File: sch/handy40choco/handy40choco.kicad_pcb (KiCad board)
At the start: 2 copper layers, 169 x 71 mm, 95 parts, among them J1 Conn_01x20, SW1 SW_Push, SW10 SW_Push, SW11 SW_Push, SW12 SW_Push, SW13 SW_Push, SW14 SW_Push, SW15 SW_Push, SW16 SW_Push, SW17 SW_Push, SW18 SW_Push, SW19 SW_Push, SW2 SW_Push, SW20 SW_Push, SW21 SW_Push, SW22 SW_Push, SW23 SW_Push, SW24 SW_Push, SW25 SW_Push, SW26 SW_Push, SW27 SW_Push, SW28 SW_Push, SW29 SW_Push, SW3 SW_Push, SW30 SW_Push, SW31 SW_Push, SW32 SW_Push, SW33 SW_Push, SW34 SW_Push, SW35 SW_Push, SW36 SW_Push, SW37 SW_Push, SW38 SW_Push, SW39 SW_Push, SW4 SW_Push, SW40 SW_Push, SW5 SW_Push, SW6 SW_Push, SW7 SW_Push, SW8 SW_Push, SW9 SW_Push

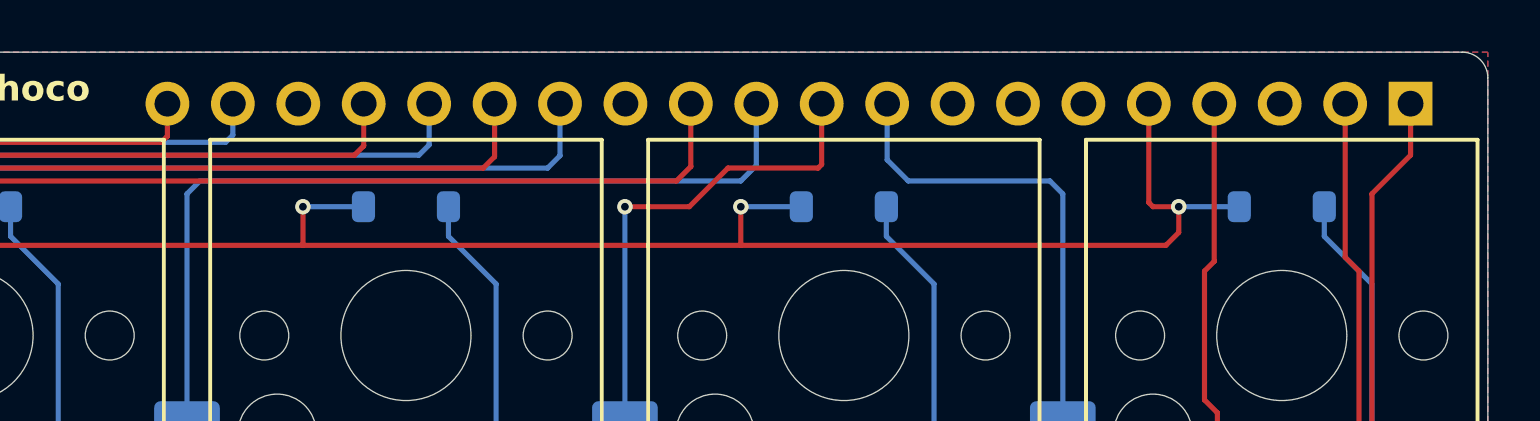
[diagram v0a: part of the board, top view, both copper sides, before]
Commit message: ピンヘッダのフットプリントをコンスルーが使えるように、Φ0.85に変更しました。
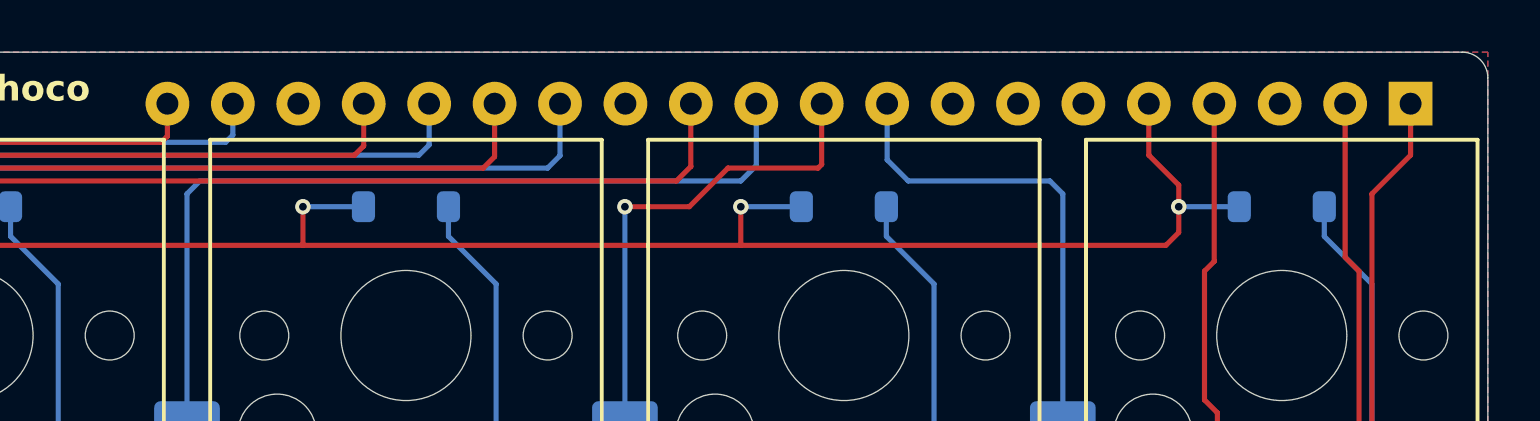
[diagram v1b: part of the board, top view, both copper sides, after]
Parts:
- J1: footprint Connector_PinHeader_2.54mm:PinHeader_1x20_P2.54mm_Vertical -> my_keyswitch:my_PinHeader_1x20_P2.54mm_Vertical_p0.85
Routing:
- net /ROW0: track 200.8 -> 200.2 mm
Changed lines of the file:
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@@
 		)
 	)
-	(footprint "Connector_PinHeader_2.54mm:PinHeader_1x20_P2.54mm_Vertical"
+	(footprint "my_keyswitch:my_PinHeader_1x20_P2.54mm_Vertical_p0.85"
 		(layer "B.Cu")
 		(at 207 88 90)
@@
 		(tags "Through hole pin header THT 1x20 2.54mm single row")
 		(property "Reference" "J1"
-			(at 0 2.38 90)
+			(at 0 2.38 270)
 			(layer "B.SilkS")
 			(effects
@@
 		)
 		(property "Value" "Conn_01x20"
-			(at 0 -50.64 90)
+			(at 0 -50.64 270)
 			(layer "B.Fab")
 			(effects
@@
 		)
 		(property "Datasheet" ""
-			(at 0 0 90)
+			(at 0 0 270)
 			(layer "B.Fab")
 			(hide yes)
@@
 		)
 		(property "Description" "Generic connector, single row, 01x20, script generated (kicad-library-utils/schlib/autogen/connector/)"
-			(at 0 0 90)
+			(at 0 0 270)
 			(layer "B.Fab")
 			(hide yes)
@@
 			(at 0 0 90)
 			(size 1.7 1.7)
-			(drill 1)
+			(drill 0.85)
 			(layers "*.Cu" "*.Mask")
 			(remove_unused_layers no)
@@
 			(at 0 -2.54 90)
 			(size 1.7 1.7)
-			(drill 1)
+			(drill 0.85)
 			(layers "*.Cu" "*.Mask")
 			(remove_unused_layers no)
@@
 			(at 0 -5.08 90)
 			(size 1.7 1.7)
-			(drill 1)
+			(drill 0.85)
 			(layers "*.Cu" "*.Mask")
 			(remove_unused_layers no)
@@
 			(at 0 -7.62 90)
 			(size 1.7 1.7)
-			(drill 1)
+			(drill 0.85)
 			(layers "*.Cu" "*.Mask")
 			(remove_unused_layers no)
@@
 			(at 0 -10.16 90)
 			(size 1.7 1.7)
-			(drill 1)
+			(drill 0.85)
 			(layers "*.Cu" "*.Mask")
 			(remove_unused_layers no)
@@
 			(at 0 -12.7 90)
 			(size 1.7 1.7)
-			(drill 1)
+			(drill 0.85)
 			(layers "*.Cu" "*.Mask")
 			(remove_unused_layers no)
@@
 			(at 0 -15.24 90)
 			(size 1.7 1.7)
-			(drill 1)
+			(drill 0.85)
 			(layers "*.Cu" "*.Mask")
 			(remove_unused_layers no)
@@
 			(at 0 -17.78 90)
 			(size 1.7 1.7)
-			(drill 1)
+			(drill 0.85)
 			(layers "*.Cu" "*.Mask")
 			(remove_unused_layers no)
@@
 			(at 0 -20.32 90)
 			(size 1.7 1.7)
-			(drill 1)
+			(drill 0.85)
 			(layers "*.Cu" "*.Mask")
 			(remove_unused_layers no)
@@
 			(at 0 -22.86 90)
 			(size 1.7 1.7)
-			(drill 1)
+			(drill 0.85)
 			(layers "*.Cu" "*.Mask")
 			(remove_unused_layers no)
@@
 			(at 0 -25.4 90)
 			(size 1.7 1.7)
-			(drill 1)
+			(drill 0.85)
 			(layers "*.Cu" "*.Mask")
 			(remove_unused_layers no)
@@
 			(at 0 -27.94 90)
 			(size 1.7 1.7)
-			(drill 1)
+			(drill 0.85)
 			(layers "*.Cu" "*.Mask")
 			(remove_unused_layers no)
@@
 			(at 0 -30.48 90)
 			(size 1.7 1.7)
-			(drill 1)
+			(drill 0.85)
 			(layers "*.Cu" "*.Mask")
 			(remove_unused_layers no)
@@
 			(at 0 -33.02 90)
 			(size 1.7 1.7)
-			(drill 1)
+			(drill 0.85)
 			(layers "*.Cu" "*.Mask")
 			(remove_unused_layers no)
@@
 			(at 0 -35.56 90)
 			(size 1.7 1.7)
-			(drill 1)
+			(drill 0.85)
 			(layers "*.Cu" "*.Mask")
 			(remove_unused_layers no)
@@
 			(at 0 -38.1 90)
 			(size 1.7 1.7)
-			(drill 1)
+			(drill 0.85)
 			(layers "*.Cu" "*.Mask")
 			(remove_unused_layers no)
@@
 			(at 0 -40.64 90)
 			(size 1.7 1.7)
-			(drill 1)
+			(drill 0.85)
 			(layers "*.Cu" "*.Mask")
 			(remove_unused_layers no)
@@
 			(at 0 -43.18 90)
 			(size 1.7 1.7)
-			(drill 1)
+			(drill 0.85)
 			(layers "*.Cu" "*.Mask")
 			(remove_unused_layers no)
@@
 			(at 0 -45.72 90)
 			(size 1.7 1.7)
-			(drill 1)
+			(drill 0.85)
 			(layers "*.Cu" "*.Mask")
 			(remove_unused_layers no)
@@
 			(at 0 -48.26 90)
 			(size 1.7 1.7)
-			(drill 1)
+			(drill 0.85)
 			(layers "*.Cu" "*.Mask")
 			(remove_unused_layers no)
@@
 			)
 			(rotate
-				(xyz -0 -0 -0)
+				(xyz 0 0 0)
 			)
 		)
@@
 			)
 			(rotate
-				(xyz -0 -180 -0)
+				(xyz -0 180 -0)
 			)
 		)
@@
 	)
 	(segment
+		(start 198 91.16)
+		(end 198 92)
+		(width 0.2)
+		(layer "F.Cu")
+		(net 44)
+	)
+	(segment
 		(start 62 93.5)
 		(end 58 93.5)
@@
 	)
 	(segment
-		(start 197 92)
-		(end 198 92)
-		(width 0.2)
-		(layer "F.Cu")
-		(net 44)
-	)
-	(segment
 		(start 96 92)
 		(end 96 93.5)
@@
 	)
 	(segment
-		(start 196.84 91.84)
-		(end 197 92)
-		(width 0.2)
-		(layer "F.Cu")
-		(net 44)
-	)
-	(segment
 		(start 62 93.5)
 		(end 79 93.5)
@@
 	)
 	(segment
+		(start 196.84 90)
+		(end 198 91.16)
+		(width 0.2)
+		(layer "F.Cu")
+		(net 44)
+	)
+	(segment
 		(start 196.84 88)
-		(end 196.84 91.84)
+		(end 196.84 90)
 		(width 0.2)
 		(layer "F.Cu")

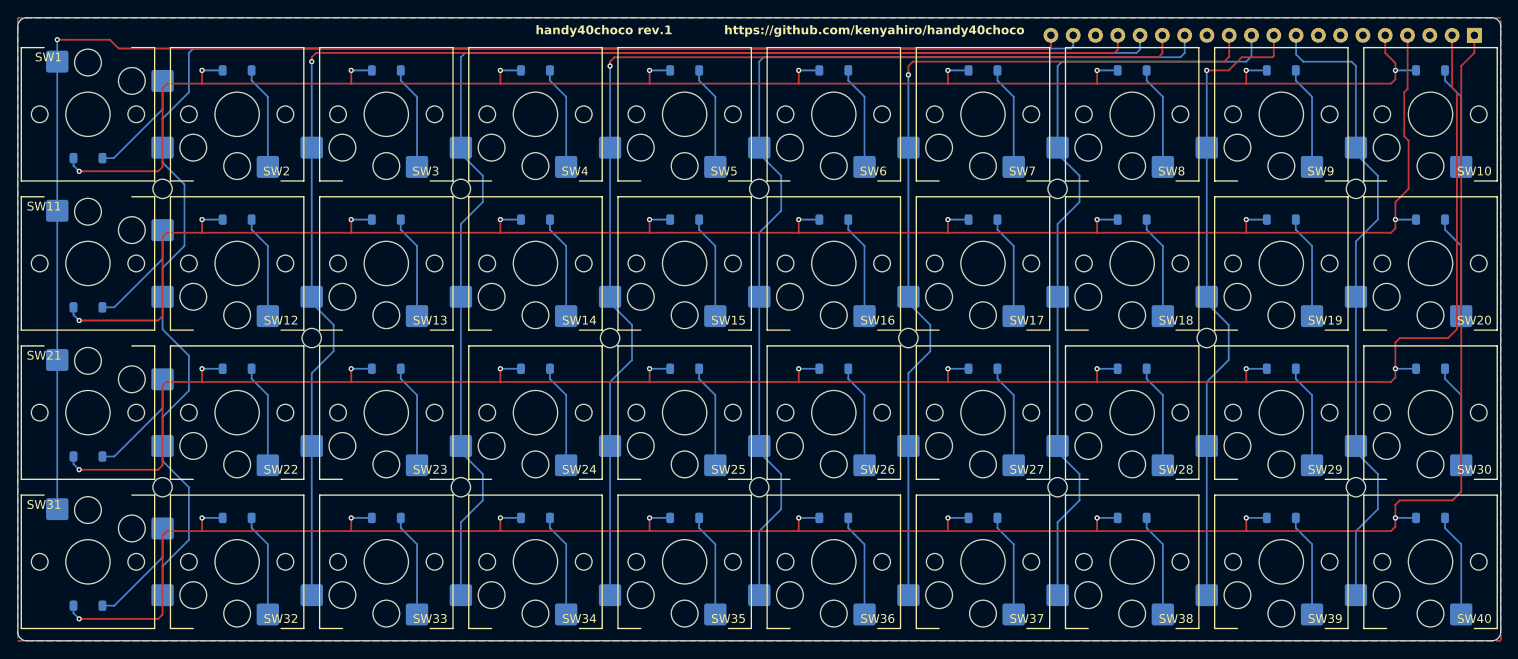
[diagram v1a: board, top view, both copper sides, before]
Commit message: マイコンのピンヘッダの位置を基板端から1.27mmに移動しました。 COLの配線を部品面に移動しました。 基板サイズの微調整を行いました。
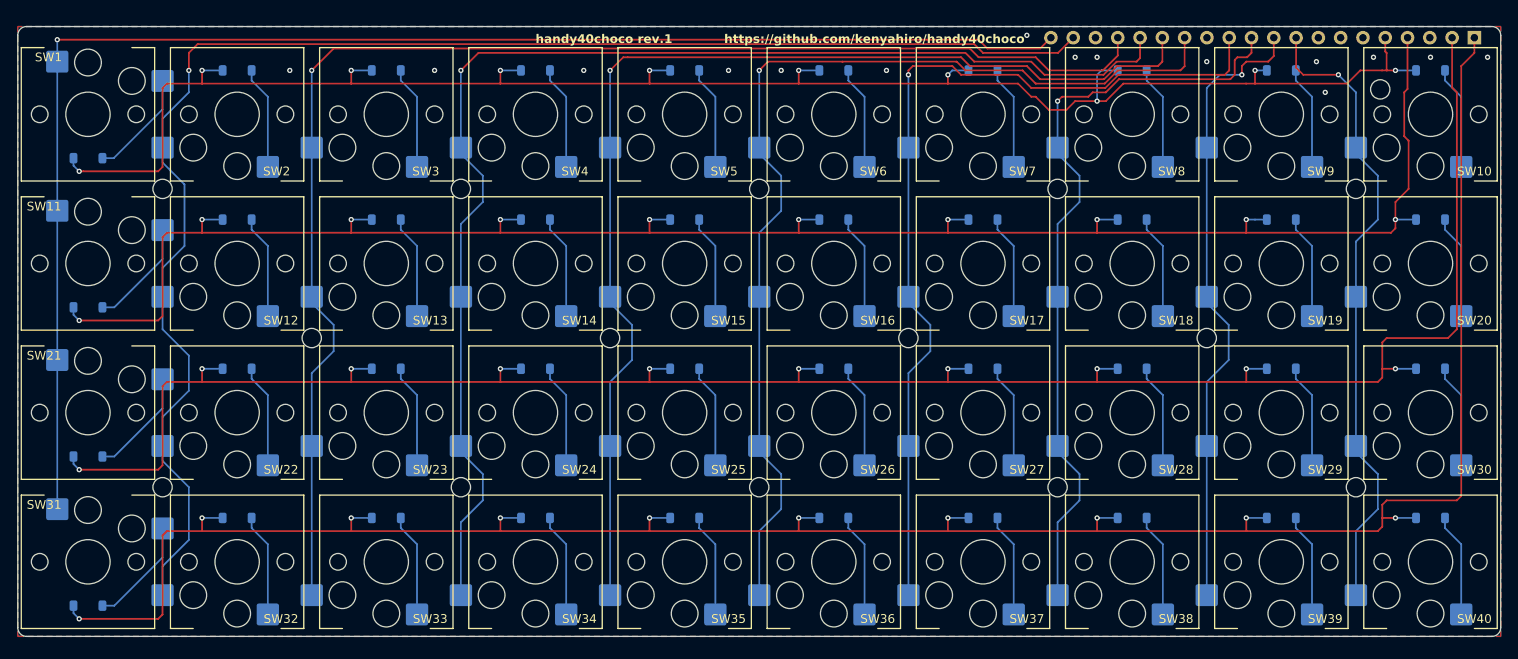
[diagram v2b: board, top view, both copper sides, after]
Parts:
- added H15: MountingHole, my_keyswitch:my_MountingHole_2.2mm_M2, F.Cu at (196.3, 94.2)
- moved J1 0.27 mm to (207.0, 88.3)
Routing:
- net /COL6: track 101.8 -> 104.2 mm
- net /COL5: track 115.8 -> 117.9 mm, vias 0 -> 1
- net /COL7: track 89.4 -> 87.5 mm, vias 0 -> 1
- net /ROW3: track 257.8 -> 259.6 mm
- net /COL4: track 128.3 -> 130.0 mm
- net /ROW0: track 200.2 -> 201.8 mm
- net /COL3: track 144.8 -> 146.3 mm, vias 0 -> 1
- net /ROW2: track 239.9 -> 241.4 mm
- net /COL2: track 157.2 -> 158.5 mm
- net /COL9: track 74.0 -> 72.8 mm, vias 0 -> 1
- net /COL8: track 72.6 -> 71.7 mm
- net /COL0: track 168.5 -> 167.7 mm
- net /COL1: vias 0 -> 1
- net GND: vias 0 -> 15
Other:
- board size 169 x 71 mm -> 169 x 69.5 mm
